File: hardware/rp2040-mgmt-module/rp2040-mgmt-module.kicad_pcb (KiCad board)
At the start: 2 copper layers, 77 x 24 mm, 88 parts, among them J1 SWD, J2 Bus_PCI_Express_x1, J3 USB_B_Micro, J4 RJ45_Hanrun_HR913550A_Horizon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, J5 ADC, J6 UART, J7 UART, SW1 BOOT, SW2 RESET, U1 W5500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

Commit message: chore: add open hardware logo
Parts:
- added REF**: OSHW-Logo2_7.3x6mm_SilkScreen, Symbol:OSHW-Logo2_7.3x6mm_SilkScreen, B.Cu at (80.7, 59.1)
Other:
- board text added: "Mgmt Module ${REVISION}"
- board text added: "POWER MANIFOLD"
- board text removed: "PDUSB"
- board text removed: "mgmt-module ${REVISION}"

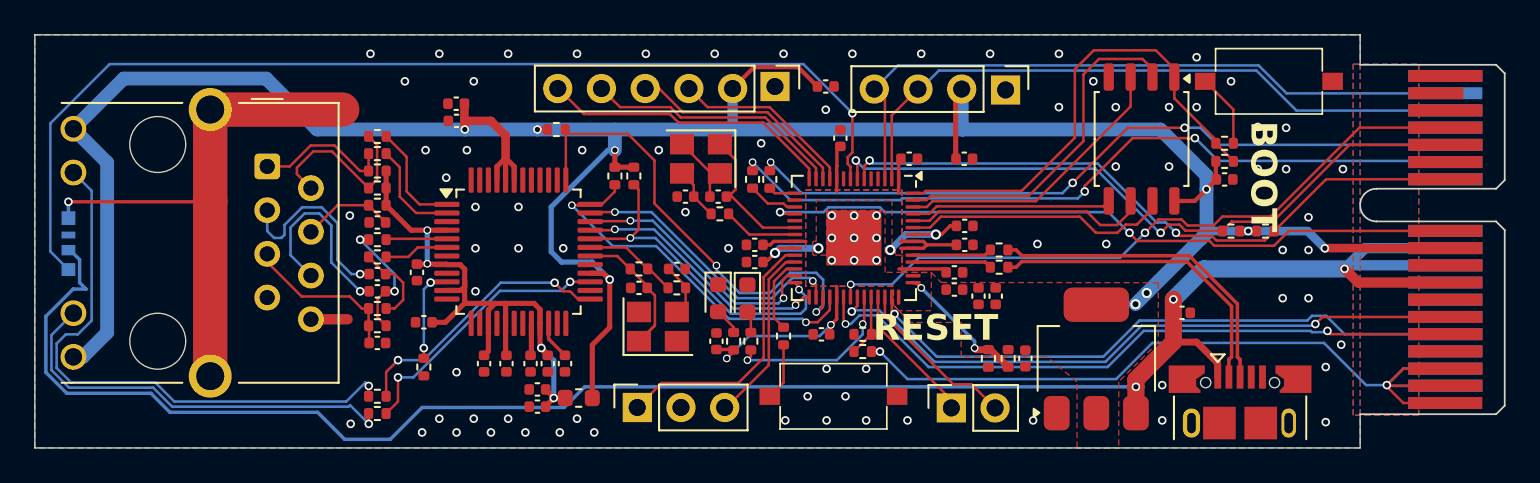
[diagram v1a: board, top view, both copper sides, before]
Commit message: fix: clean up traces
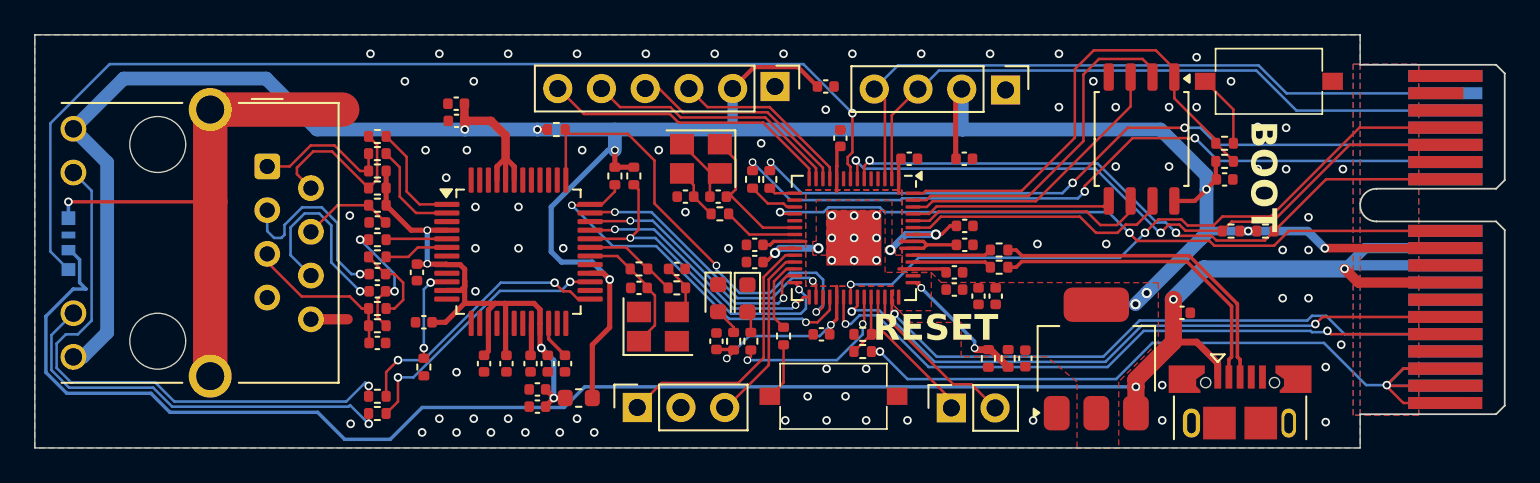
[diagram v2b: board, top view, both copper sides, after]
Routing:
- net Net-(U1-XI/CLKIN): track 9.17 -> 7.71 mm
- net +3.3V: track 186.0 -> 185.1 mm
- net Net-(C4-Pad1): track 3.12 -> 2.29 mm
- net /QSPI_SS: track 28.2 -> 27.5 mm
- net /GPIO21: track 22.1 -> 21.4 mm
- net /QSPI_SCLK: track 14.1 -> 13.5 mm
- net Net-(J4-RCT): track 9.50 -> 8.98 mm
- net GND: track 39.0 -> 38.5 mm
